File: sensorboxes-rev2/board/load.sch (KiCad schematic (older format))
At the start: 0 parts

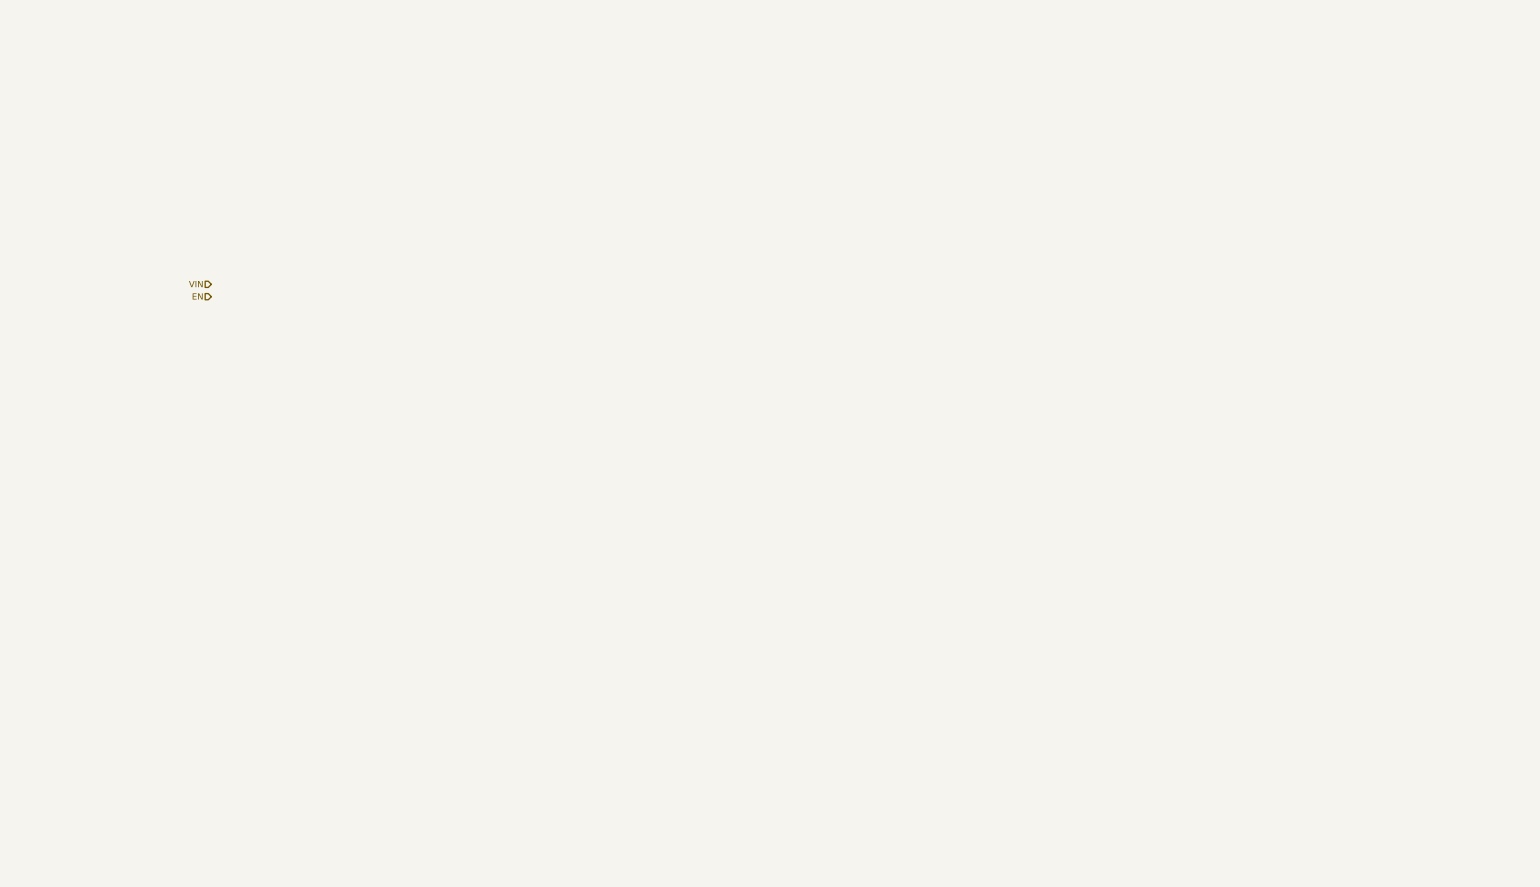
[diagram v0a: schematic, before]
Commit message: added symbols for buck converter & boost converter + preliminary schematic for the overall system architecture.
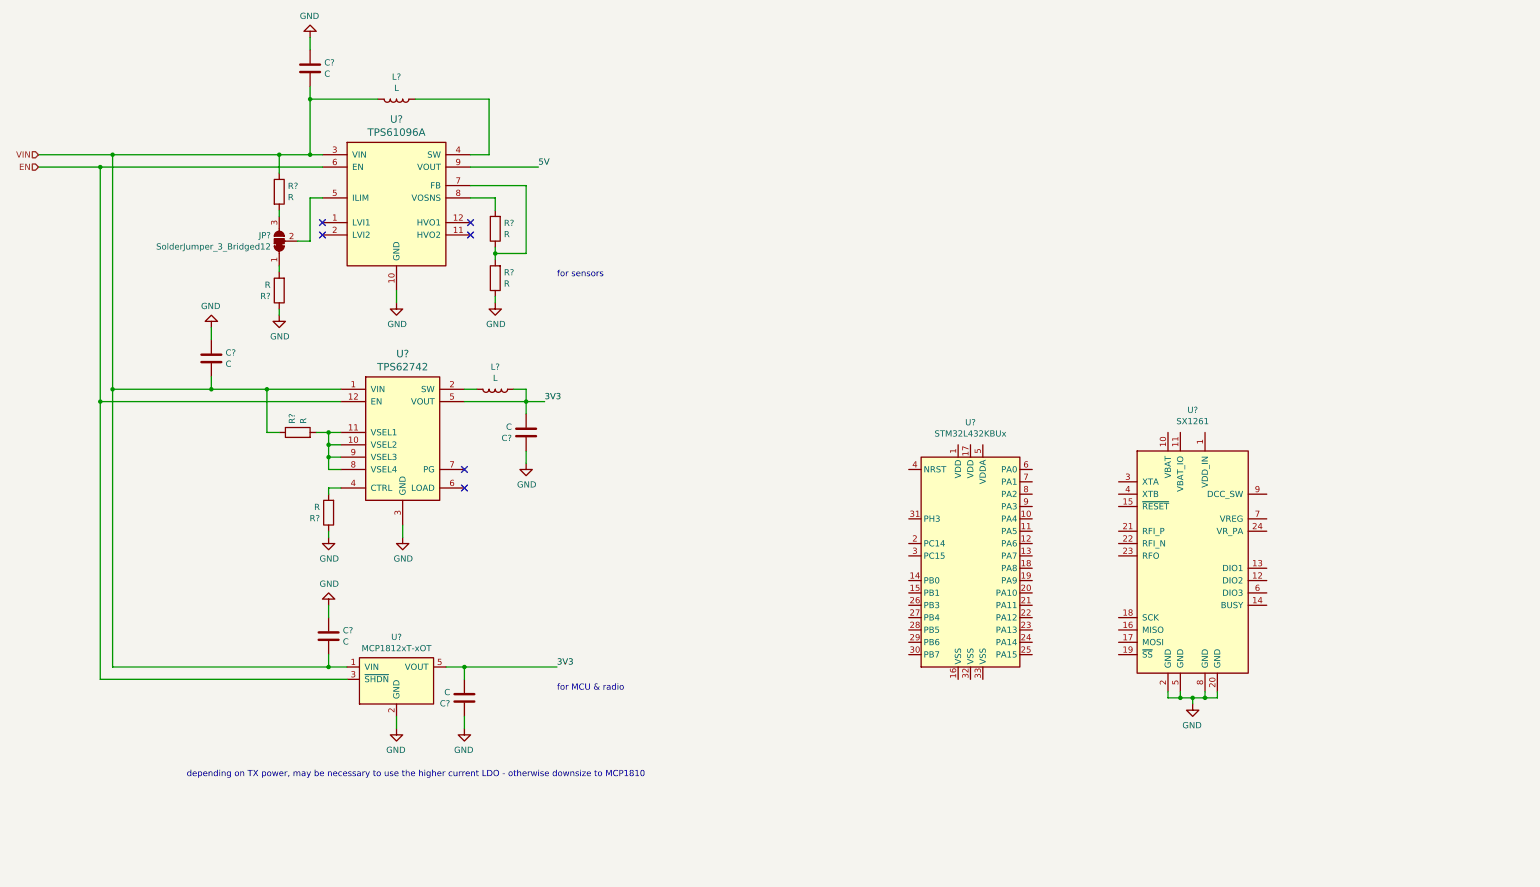
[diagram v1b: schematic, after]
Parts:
- added C? (x5): C, symbol Device:C
- added JP?: SolderJumper_3_Bridged12, symbol Jumper:SolderJumper_3_Bridged12
- added L? (x2): L, symbol Device:L
- added R? (x6): R, symbol Device:R
- added U?: TPS61096A, Package_SON:WSON-12-1EP_3x2mm_P0.5mm_EP1x2.65, symbol wsn_sds_design_symbols:TPS61096A
- added U?: TPS62742, Package_SON:WSON-12-1EP_3x2mm_P0.5mm_EP1x2.65, symbol wsn_sds_design_symbols:TPS62742
- added U?: MCP1812xT-xOT, Package_TO_SOT_SMD:SOT-23-5, symbol wsn_sds_design_symbols:MCP1812xT-xOT
- added U?: SX1261, Package_DFN_QFN:QFN-24-1EP_4x4mm_P0.5mm_EP2.6x2.6mm, symbol wsn_sds_design_symbols:SX1261
- added U?: STM32L432KBUx, Package_DFN_QFN:QFN-32-1EP_5x5mm_P0.5mm_EP3.45x3.45mm, symbol MCU_ST_STM32L4:STM32L432KBUx
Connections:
- net EN: now also U?.12 (EN), U?.3 (~SHDN), U?.6 (EN)
- net VIN: now also C?.2, C?.2, C?.2, L?.2, R?.1, R?.1, U?.1 (VIN), U?.1 (VIN), U?.3 (VIN)
- new net: L?.1, U?.4 (SW)
- new net: JP?.2 (C), U?.5 (ILIM)
- new net: R?.1, R?.2, U?.7 (FB)
- new net: R?.2, U?.8 (VOSNS)
- new net: R?.2, U?.10 (VSEL2), U?.11 (VSEL1), U?.8 (VSEL4), U?.9 (VSEL3)
- new net: L?.2, U?.2 (SW)
- new net: R?.2, U?.4 (CTRL)
- new net: JP?.1 (A), R?.2
- new net: JP?.3 (B), R?.2
- new net 3V3: C?.2, C?.2, L?.1, U?.5 (VOUT), U?.5 (VOUT)
- new net 5V: U?.9 (VOUT)
- new net GND: C?.1, C?.1, C?.1, C?.1, C?.1, R?.1, R?.1, R?.1, U?.10 (GND), U?.2 (GND), U?.2 (GND), U?.20 (GND), U?.3 (GND), U?.5 (GND), U?.8 (GND)
- no-connect marks 0 -> 6
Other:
- note added: "depending on TX power, may be necessary to use the higher current LDO - otherwise downsize to MCP1810"
- note added: "for MCU & radio"
- note added: "for sensors"

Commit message: yeah
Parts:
- added C? (x4): C, symbol Device:C
- added R? (x2): R, symbol Device:R
- added U? (x2): SiP32431DR3, Package_TO_SOT_SMD:SOT-363_SC-70-6, symbol wsn_sds_design_symbols:SiP32431DR3
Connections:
- net 3V3: now also C?.2, U?.4 (IN)
- net 5V: now also C?.2, U?.4 (IN)
- net GND: now also C?.1, C?.1, C?.1, C?.1, R?.2, R?.2, U?.2 (GND), U?.2 (GND), U?.5 (GND), U?.5 (GND)
- new net sensor: C?.2, C?.2, R?.1, R?.1, U?.1 (OUT), U?.1 (OUT)
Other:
- note added: "MCU control signals"

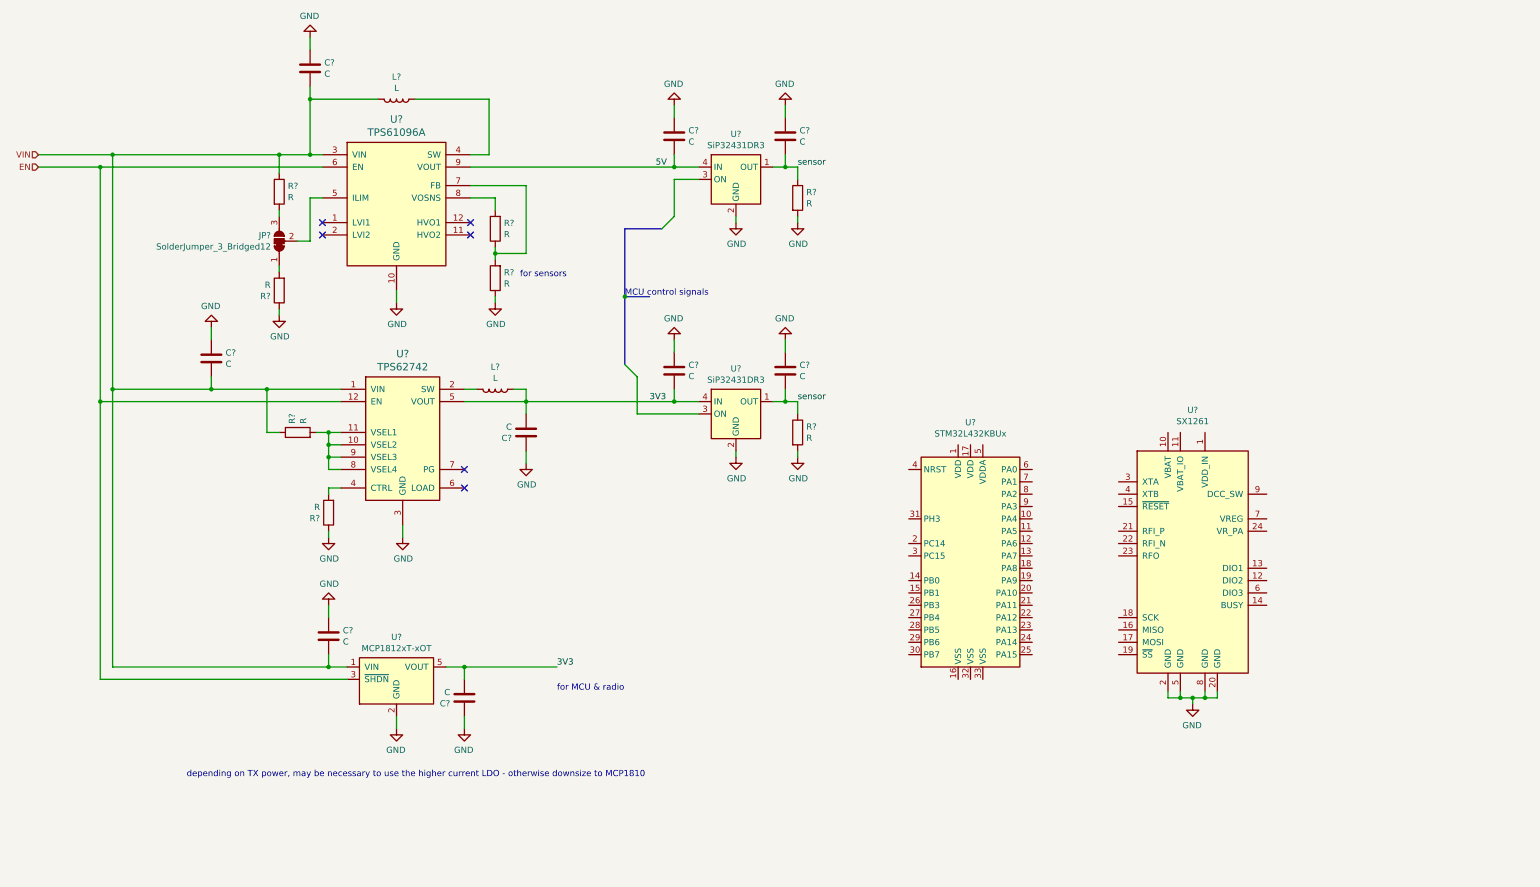
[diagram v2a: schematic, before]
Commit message: developed more of the schematic for the STM32 + radio. also picked out passives & figured out bidirectional battery polarity checking + reverse polarity protection for the solar panel.
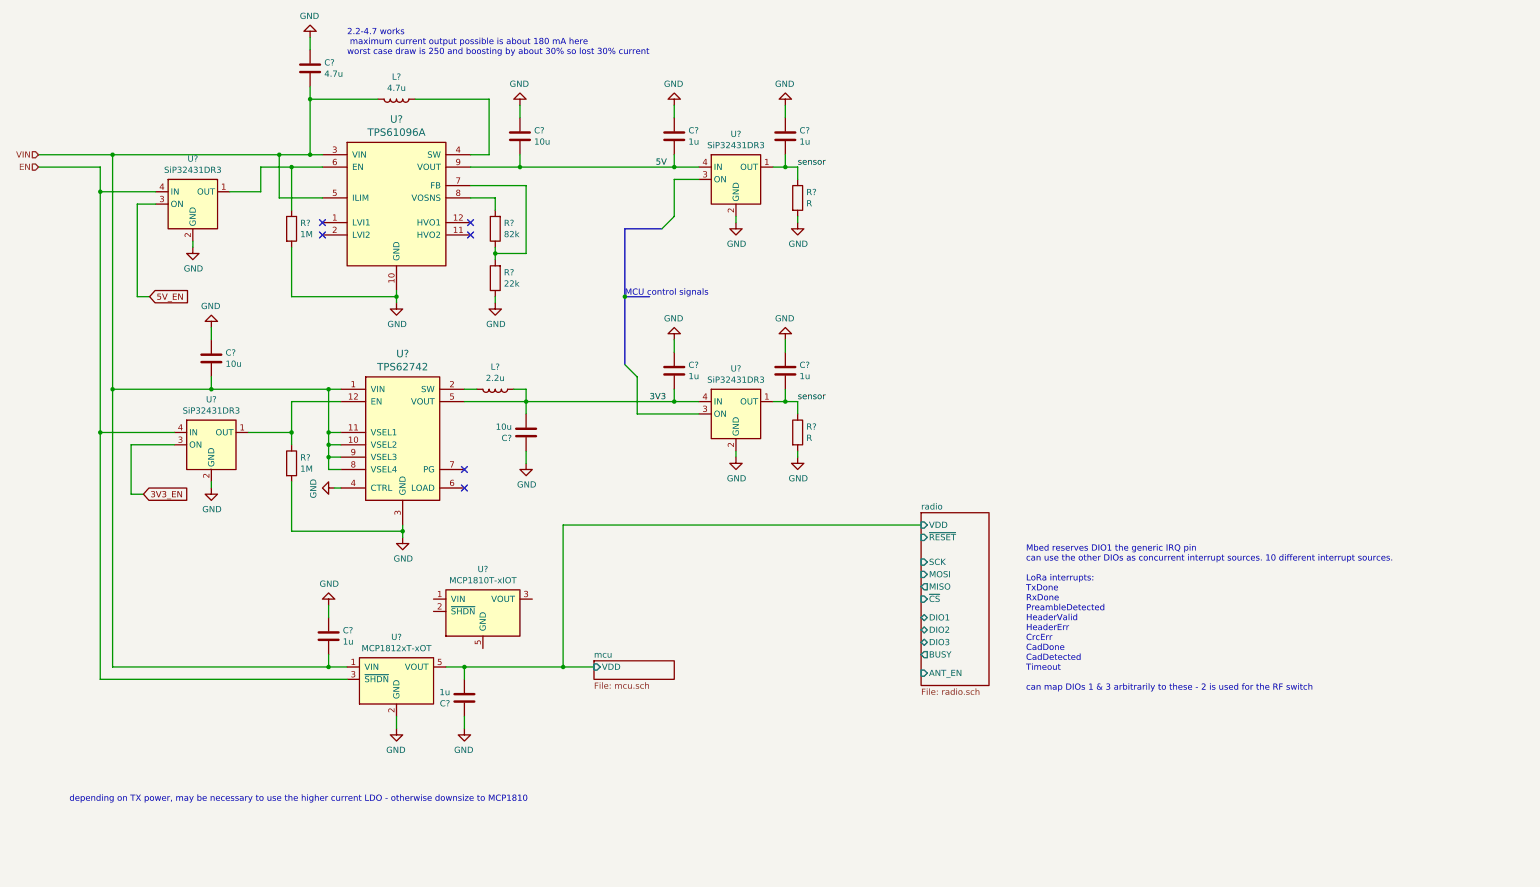
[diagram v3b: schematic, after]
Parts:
- removed JP?: SolderJumper_3_Bridged12, symbol Jumper:SolderJumper_3_Bridged12
- removed R? (x4): R, symbol Device:R
- removed U?: SX1261, Package_DFN_QFN:QFN-24-1EP_4x4mm_P0.5mm_EP2.6x2.6mm, symbol wsn_sds_design_symbols:SX1261
- removed U?: STM32L432KBUx, Package_DFN_QFN:QFN-32-1EP_5x5mm_P0.5mm_EP3.45x3.45mm, symbol MCU_ST_STM32L4:STM32L432KBUx
- added C?: 10u, symbol Device:C
- added R? (x2): 1M, symbol Device:R
- added U?: MCP1810T-xIOT, Package_TO_SOT_SMD:SOT-23-5, symbol wsn_sds_design_symbols:MCP1810T-xIOT
- added U? (x2): SiP32431DR3, Package_TO_SOT_SMD:SOT-363_SC-70-6, symbol wsn_sds_design_symbols:SiP32431DR3
- C? (x6): value C -> 1u
- C?: value C -> 4.7u
- C? (x2): value C -> 10u
- L?: value L -> 4.7u
- L?: value L -> 2.2u
- R?: value R -> 82k
- R?: value R -> 22k
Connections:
- net 3V3: no longer C?.2, U?.5 (VOUT)
- net 5V: now also C?.2
- net EN: now also U?.4 (IN), U?.4 (IN); no longer U?.12 (EN), U?.6 (EN)
- net GND: now also U?.4 (CTRL), C?.1, R?.2, R?.2, U?.2 (GND), U?.2 (GND), U?.5 (GND), U?.5 (GND)
- net VIN: now also U?.10 (VSEL2), U?.11 (VSEL1), U?.5 (ILIM), U?.8 (VSEL4), U?.9 (VSEL3)
- new net: R?.1, U?.1 (OUT), U?.6 (EN)
- new net: R?.1, U?.1 (OUT), U?.12 (EN)
- new net 3V3_EN: U?.3 (ON)
- new net 5V_EN: U?.3 (ON)
- new net mcu/VDD: C?.2, U?.5 (VOUT)
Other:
- note added: "2.2-4.7 works\n maximum current output possible is about 180 mA here \nworst case draw is 250 and boosting by about 30% so lost 30% current"
- note added: "Mbed reserves DIO1 the generic IRQ pin\ncan use the other DIOs as concurrent interrupt sources. 10 different interrupt sources.\n\nLoRa interrupts:\nTxDone\nRxDone\nPreambleDetected\nHeaderValid\nHeaderErr\nCrcErr\nCadDone\nCadDetected\nTimeout\n\ncan map DIOs 1 & 3 arbitrarily to these - 2 is used for the RF switch\n"
- note removed: "for MCU & radio"
- note removed: "for sensors"

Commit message: exposing pins for mcu, added part values for RF section
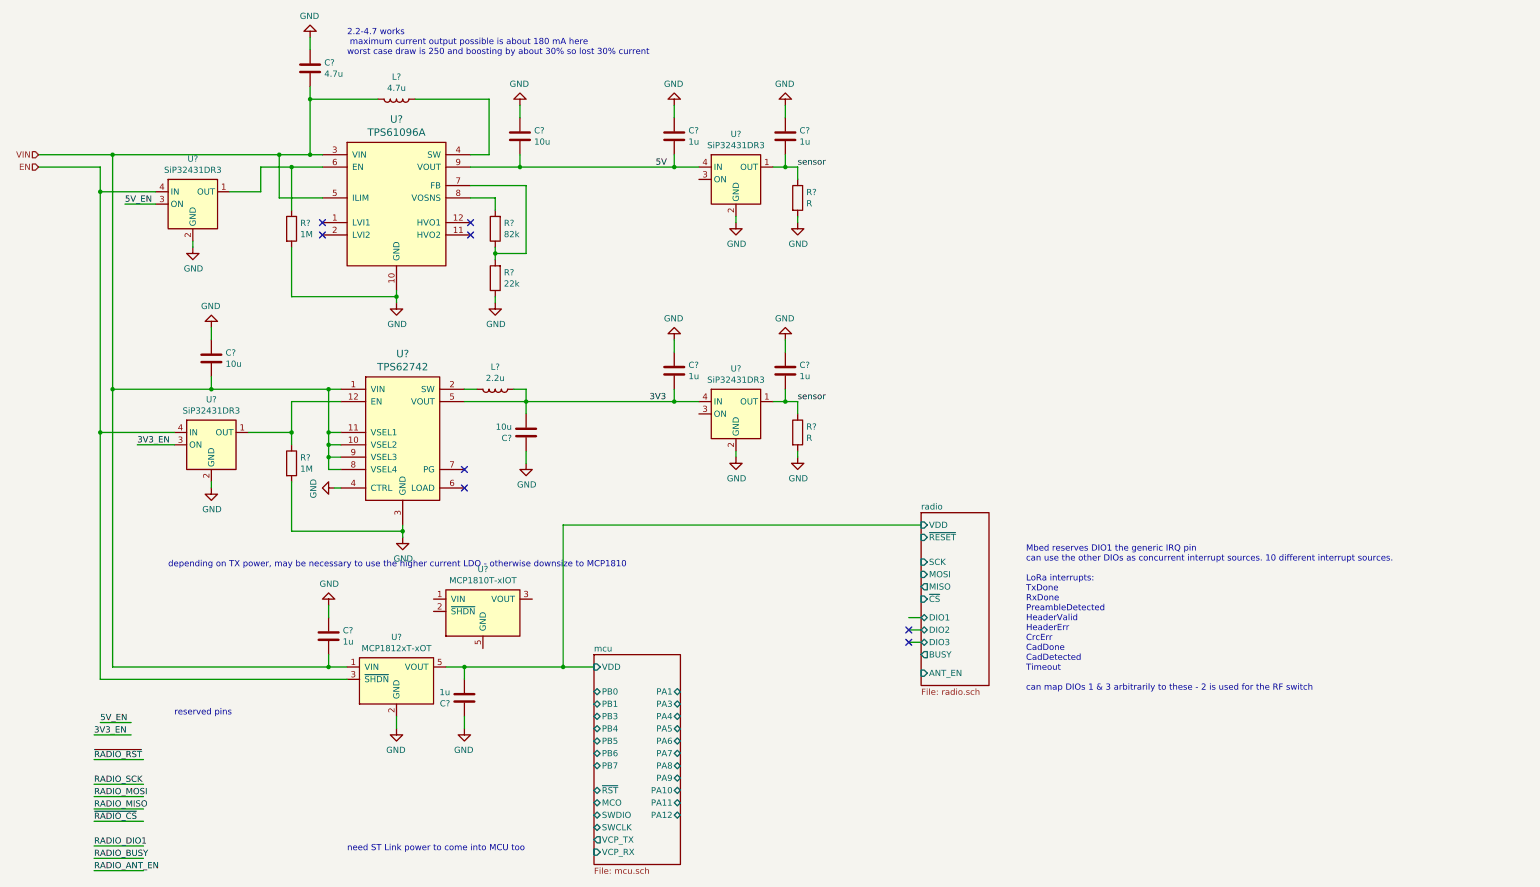
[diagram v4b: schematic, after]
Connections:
- net labels added: RADIO_ANT_EN, RADIO_BUSY, RADIO_DIO1, RADIO_MISO, RADIO_MOSI, RADIO_SCK, ~RADIO_CS, ~RADIO_RST
- wire segments 116 -> 121
- no-connect marks 6 -> 8
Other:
- note added: "need ST Link power to come into MCU too"
- note added: "reserved pins"
- note removed: "MCU control signals"
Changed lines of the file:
@@
 $EndComp
 Connection ~ 3200 5950
-Text Notes 1100 7050 0    50   ~ 0
+Text Notes 1900 5150 0    50   ~ 0
 depending on TX power, may be necessary to use the higher current LDO - otherwise downsize to MCP1810
 Wire Wire Line
@@
 	1    0    0    -1
 $EndComp
-Entry Wire Line
-	5600 3500 5700 3600
-Wire Wire Line
-	5700 3600 5700 3900
-Entry Wire Line
-	5900 2400 6000 2300
-Wire Wire Line
-	6000 2300 6000 2000
-Wire Bus Line
-	5900 2400 5600 2400
-Text Notes 5600 2950 0    50   ~ 0
-MCU control signals
-Wire Bus Line
-	5600 2400 5600 2950
-Wire Bus Line
-	5600 2950 5800 2950
-Connection ~ 5600 2950
-Wire Bus Line
-	5600 2950 5600 3500
 Wire Wire Line
 	6000 1900 6200 1900
 Wire Wire Line
-	6000 2000 6200 2000
-Wire Wire Line
 	6000 3800 6200 3800
-Wire Wire Line
-	5700 3900 6200 3900
 Text Notes 8850 6150 0    50   ~ 0
 Mbed reserves DIO1 the generic IRQ pin\ncan use the other DIOs as concurrent interrupt sources. 10 different interrupt sources.\n\nLoRa interrupts:\nTxDone\nRxDone\nPreambleDetected\nHeaderValid\nHeaderErr\nCrcErr\nCadDone\nCadDetected\nTimeout\n\ncan map DIOs 1 & 3 arbitrarily to these - 2 is used for the RF switch\n
@@
 $EndComp
 $Sheet
-S 5350 5900 650  150
+S 5350 5850 700  1700
 U 5E59DFEA
 F0 "mcu" 50
 F1 "mcu.sch" 50
 F2 "VDD" I L 5350 5950 50
+F3 "PA1" B R 6050 6150 50
+F4 "PA3" B R 6050 6250 50
+F5 "PA4" B R 6050 6350 50
+F6 "PA5" B R 6050 6450 50
+F7 "PA6" B R 6050 6550 50
+F8 "PA7" B R 6050 6650 50
+F9 "PA8" B R 6050 6750 50
+F10 "PA9" B R 6050 6850 50
+F11 "PA10" B R 6050 6950 50
+F12 "PA11" B R 6050 7050 50
+F13 "PA12" B R 6050 7150 50
+F14 "MCO" B L 5350 7050 50
+F15 "VCP_TX" O L 5350 7350 50
+F16 "SWDIO" B L 5350 7150 50
+F17 "SWCLK" B L 5350 7250 50
+F18 "VCP_RX" I L 5350 7450 50
+F19 "PB0" B L 5350 6150 50
+F20 "PB1" B L 5350 6250 50
+F21 "PB3" B L 5350 6350 50
+F22 "PB4" B L 5350 6450 50
+F23 "PB5" B L 5350 6550 50
+F24 "PB6" B L 5350 6650 50
+F25 "PB7" B L 5350 6750 50
+F26 "~RST" B L 5350 6950 50
 $EndSheet
 $Sheet
@@
 $EndComp
 Wire Wire Line
-	1800 2200 1650 2200
-Wire Wire Line
-	1650 2200 1650 2950
-Text GLabel 1750 2950 2    50   Input ~ 0
-5V_EN
-Wire Wire Line
-	1750 2950 1650 2950
-Text GLabel 1700 4550 2    50   Input ~ 0
-3V3_EN
-Wire Wire Line
-	1700 4550 1600 4550
-Wire Wire Line
-	1600 4550 1600 4150
-Wire Wire Line
-	1600 4150 1950 4150
-Wire Wire Line
 	5350 5950 5100 5950
 Connection ~ 5100 5950
+Text Notes 3350 7450 0    50   ~ 0
+need ST Link power to come into MCU too
+Wire Wire Line
+	1800 2200 1550 2200
+Text Label 1550 2200 0    50   ~ 0
+5V_EN
+Wire Wire Line
+	1950 4150 1650 4150
+Text Label 1650 4150 0    50   ~ 0
+3V3_EN
+Wire Wire Line
+	1600 6500 1300 6500
+Text Label 1300 6500 0    50   ~ 0
+3V3_EN
+Wire Wire Line
+	1600 6400 1350 6400
+Text Label 1350 6400 0    50   ~ 0
+5V_EN
+Text Notes 1950 6350 0    50   ~ 0
+reserved pins
+Text Label 1300 6700 0    50   ~ 0
+~RADIO_RST
+Wire Wire Line
+	1300 6700 1700 6700
+Wire Wire Line
+	1300 7200 1700 7200
+Text Label 1300 7200 0    50   ~ 0
+~RADIO_CS
+Wire Wire Line
+	1300 6900 1700 6900
+Text Label 1300 6900 0    50   ~ 0
+RADIO_SCK
+Wire Wire Line
+	1300 7000 1700 7000
+Text Label 1300 7000 0    50   ~ 0
+RADIO_MOSI
+Wire Wire Line
+	1300 7100 1700 7100
+Text Label 1300 7100 0    50   ~ 0
+RADIO_MISO
+Wire Wire Line
+	8000 5650 7900 5650
+NoConn ~ 7900 5650
+Wire Wire Line
+	8000 5750 7900 5750
+NoConn ~ 7900 5750
+Wire Wire Line
+	8000 5550 7900 5550
+Text Label 1300 7400 0    50   ~ 0
+RADIO_DIO1
+Wire Wire Line
+	1300 7400 1700 7400
+Text Label 1300 7500 0    50   ~ 0
+RADIO_BUSY
+Wire Wire Line
+	1300 7500 1700 7500
+Text Label 1300 7600 0    50   ~ 0
+RADIO_ANT_EN
+Wire Wire Line
+	1300 7600 1700 7600
 $EndSCHEMATC
